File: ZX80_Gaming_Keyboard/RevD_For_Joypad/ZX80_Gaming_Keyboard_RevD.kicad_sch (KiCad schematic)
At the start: 47 parts, among them J1 KB1, J3 KB2, J4 ZX81 Joypad, SW1 1, SW10 E, SW11 D, SW12 X, SW13 4, SW14 R, SW15 F, SW16 C, SW17 5, SW18 T, SW19 G, SW2 Q, SW20 V, SW21 6, SW22 Y, SW23 H, SW24 B, SW25 7, SW26 U, SW27 J, SW28 N, SW29 8, SW3 A, SW30 I, SW31 K, SW32 M, SW33 9, SW34 O, SW35 L, SW36 DOT, SW37 0, SW38 P, SW39 NL, SW4 SHIFT, SW40 SPACE, SW5 2, SW6 W, SW7 S, SW8 Z, SW9 3

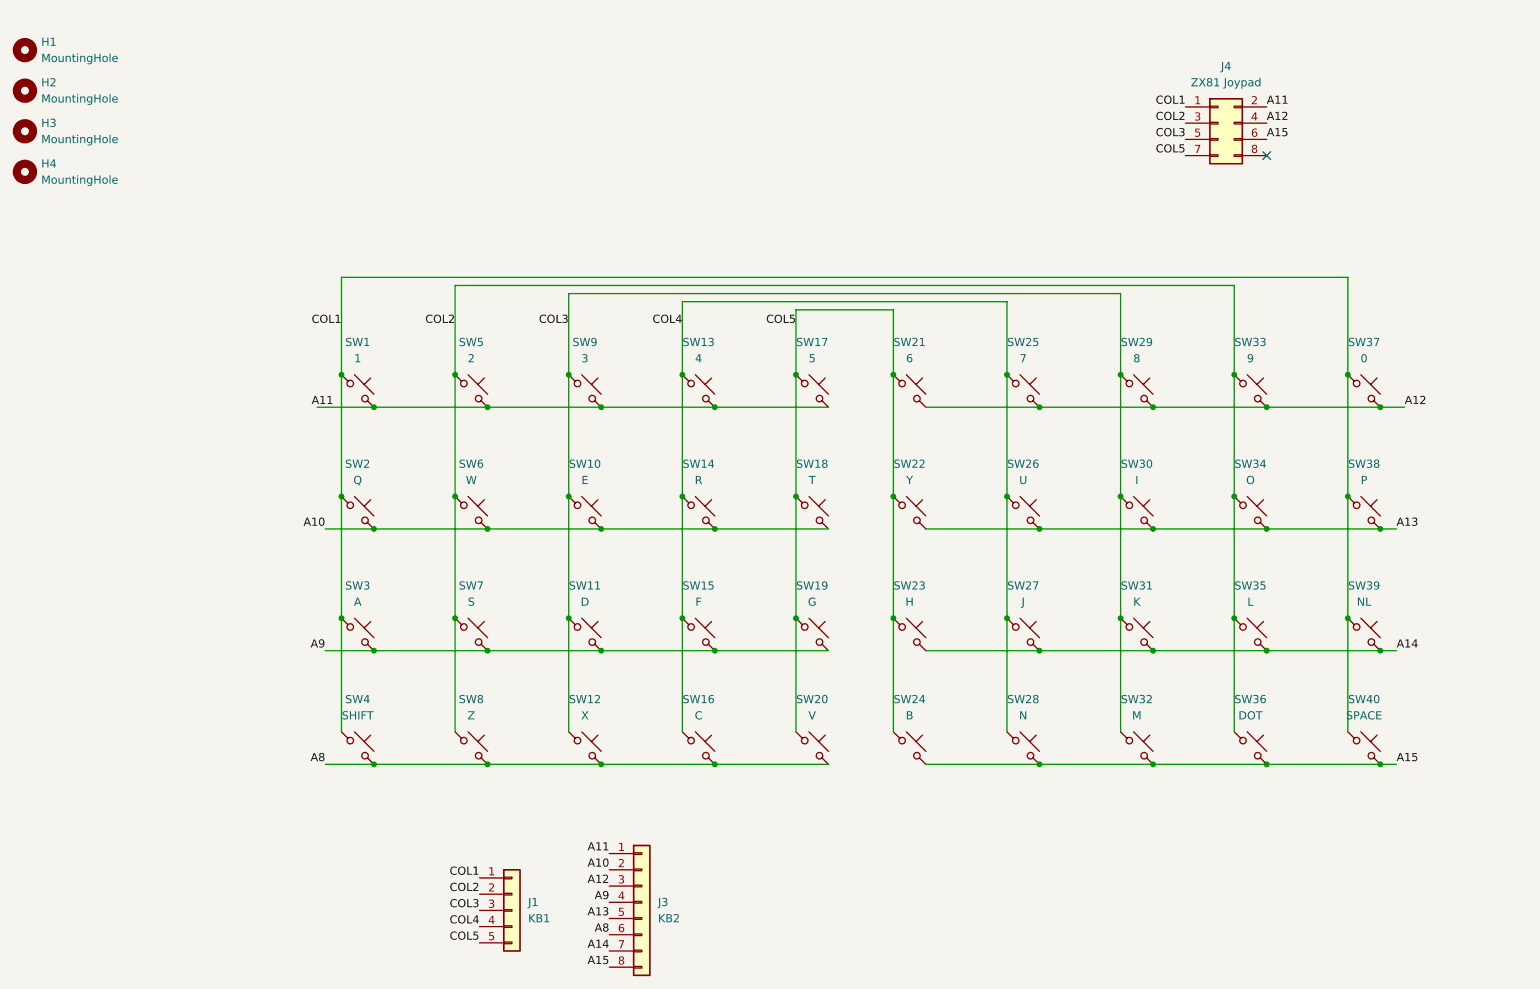
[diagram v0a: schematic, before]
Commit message: Corrected footprint spacing
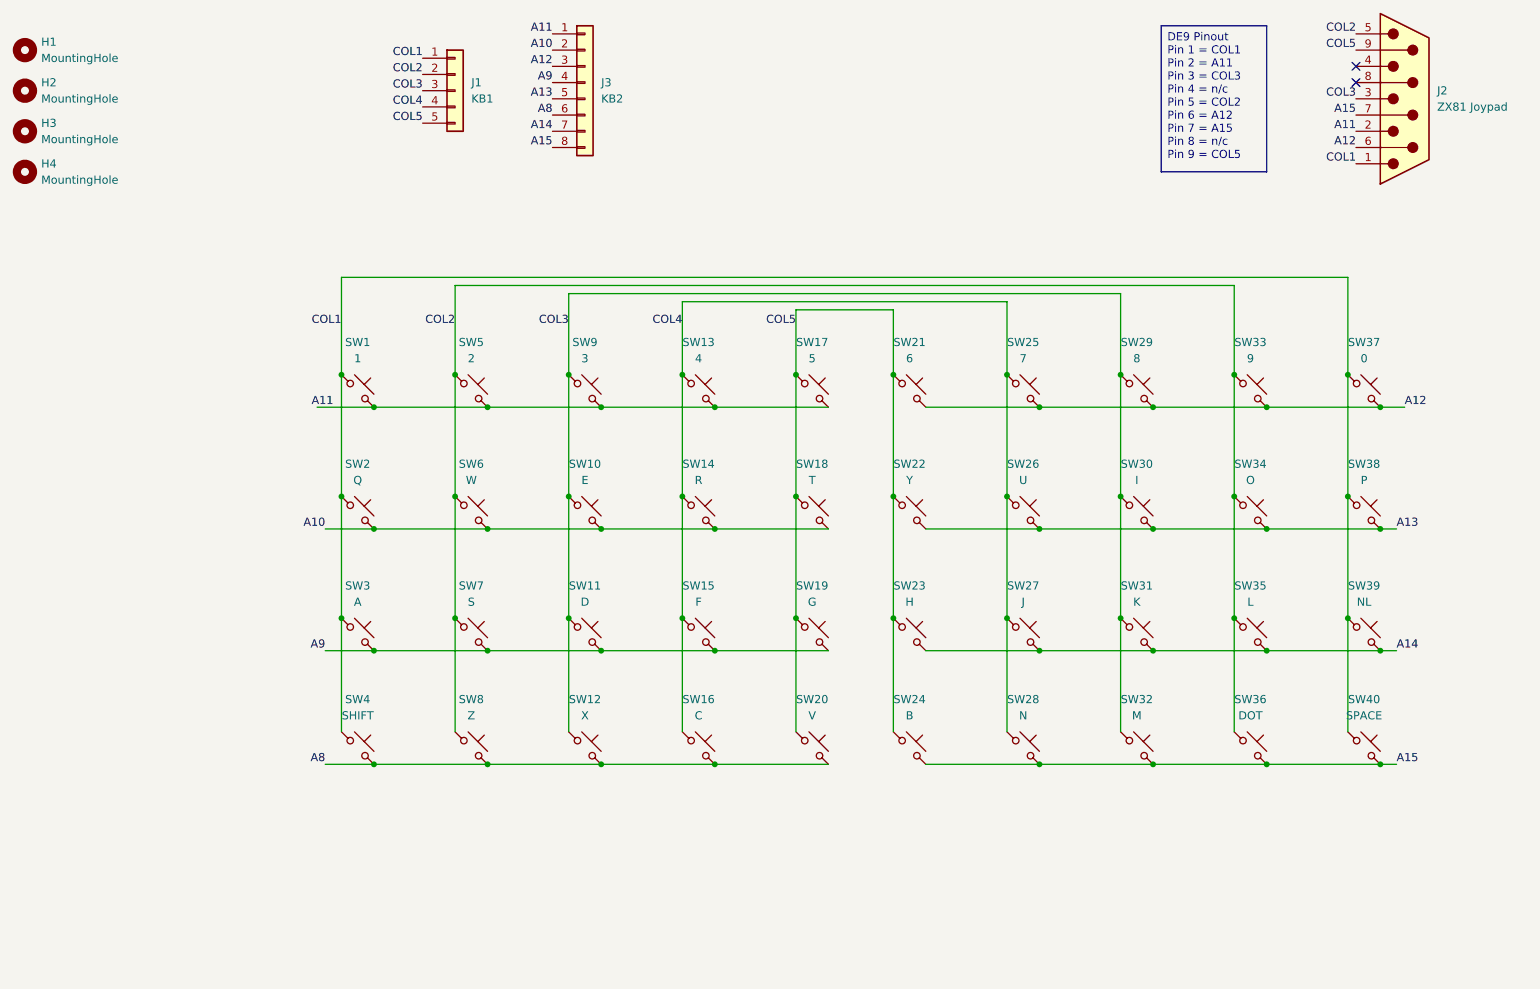
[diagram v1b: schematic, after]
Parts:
- removed J4: ZX81 Joypad, Connector_PinHeader_2.54mm:PinHeader_2x04_P2.54mm_Vertical, symbol Connector_Generic:Conn_02x04_Odd_Even
- added J2: ZX81 Joypad, Connector_Dsub:DSUB-9_Pins_EdgeMount_P2.77mm, symbol Connector:DE9_Pins
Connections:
- net A11: now also J2.2
- net A12: now also J2.6
- net A15: now also J2.7
- net COL1: now also J2.1
- net COL2: now also J2.5
- net COL3: now also J2.3
- net COL5: now also J2.9
- no-connect marks 1 -> 2
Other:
- title: ZX80 Gaming Keyboard -> ZX81 Gaming Keyboard
- moved on the sheet: J1, J3
